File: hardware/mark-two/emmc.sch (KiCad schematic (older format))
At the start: 21 parts, among them U2 MX6UL-VM, U3 EMMC16G

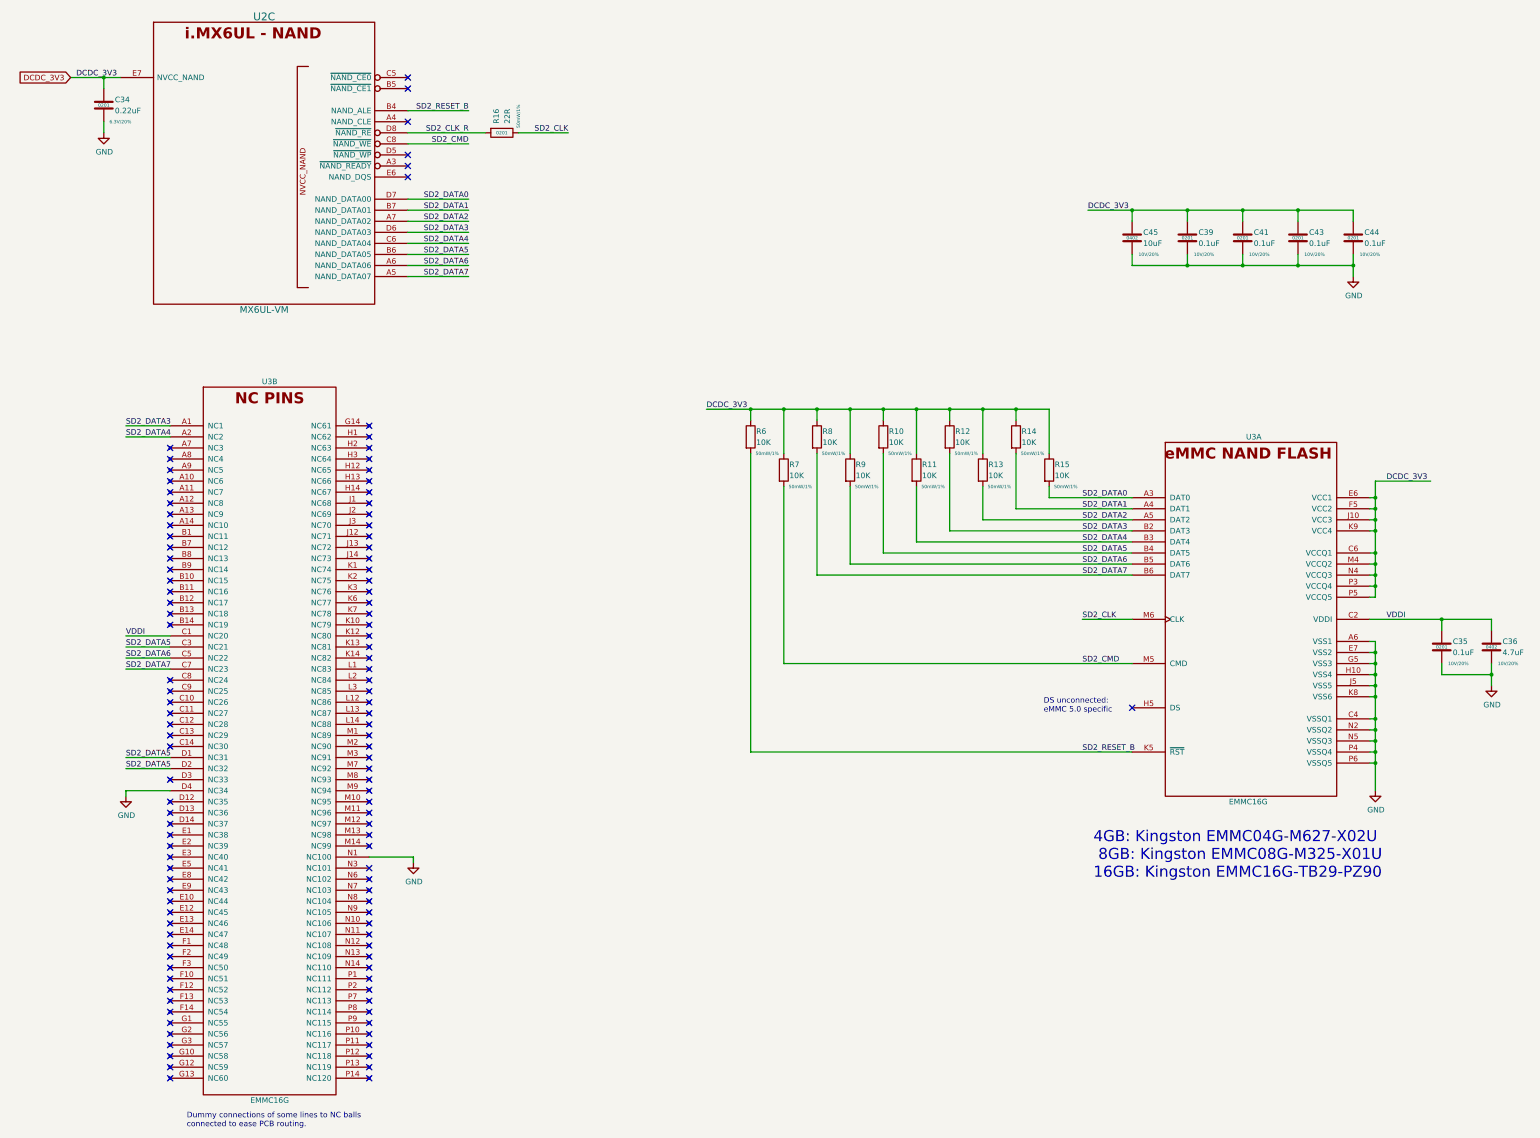
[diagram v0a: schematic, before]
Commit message: add USB armory Mk II rev. γ
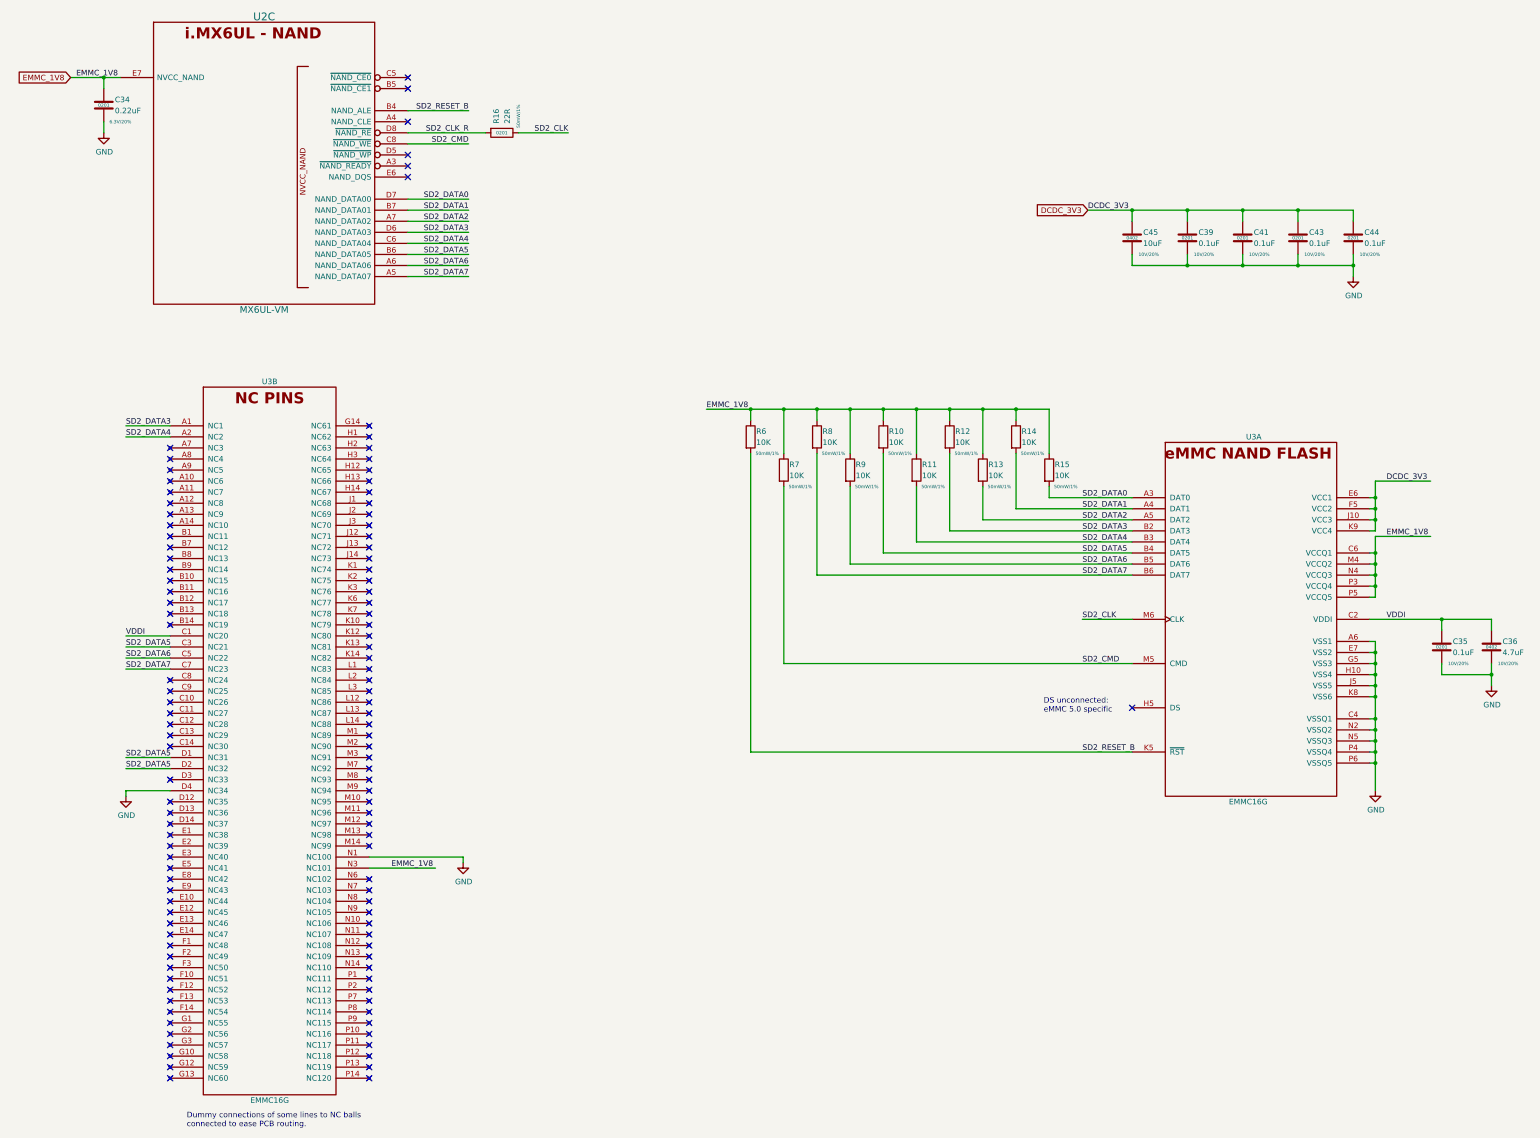
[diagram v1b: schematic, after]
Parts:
- U2: Mfg PN (none) -> MCIMX6Z0DVM09AB
- U3: Alternative PN (none) -> FEMDNN016G-58A43, FEMDRM016G-58A43
- U3: Alternative PN (none) -> FEMDNN016G-58A43, FEMDRM016G-58A43; Mfg PN (none) -> EMMC16G-TB29-PZ90
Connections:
- net DCDC_3V3: no longer C34.1, R10.1, R11.1, R12.1, R13.1, R14.1, R15.1, R6.1, R7.1, R8.1, R9.1, U2.E7 (NVCC_NAND), U3.C6 (VCCQ1), U3.M4 (VCCQ2), U3.N4 (VCCQ3), U3.P3 (VCCQ4), U3.P5 (VCCQ5)
- net EMMC_1V8: now reaches U3.N3 (NC101)
- net EMMC_1V8: now also C34.1, R10.1, R11.1, R12.1, R13.1, R14.1, R15.1, R6.1, R7.1, R8.1, R9.1, U2.E7 (NVCC_NAND), U3.C6 (VCCQ1), U3.M4 (VCCQ2), U3.N4 (VCCQ3), U3.P3 (VCCQ4), U3.P5 (VCCQ5)
- no-connect marks 117 -> 116
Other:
- note removed: "4GB: Kingston EMMC04G-M627-X02U\n 8GB: Kingston EMMC08G-M325-X01U\n16GB: Kingston EMMC16G-TB29-PZ90"
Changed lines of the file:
@@
 EESchema Schematic File Version 4
-LIBS:armory-cache
 EELAYER 30 0
 EELAYER END
@@
 encoding utf-8
 Sheet 3 13
-Title "USB ARMORY"
-Date "2019-06-25"
-Rev "MARK II"
+Title "USB armory Mk II"
+Date "2021-02-18"
+Rev "γ"
 Comp "F-Secure"
-Comment1 "Copyright © 2019 F-Secure"
-Comment2 "License: CERN OHL v1.2"
-Comment3 "https://github.com/inversepath/usbarmory"
+Comment1 "Copyright © F-Secure Corporation"
+Comment2 "License: CERN-OHL-S"
+Comment3 "https://github.com/f-secure-foundry/usbarmory"
 Comment4 ""
 $EndDescr
@@
 F 7 "Avnet" H 12350 4650 50  0001 C CNN "Supplier"
 F 8 "-" H 12350 4650 50  0001 C CNN "Supplier PN"
+F 9 "FEMDNN016G-58A43, FEMDRM016G-58A43 " H 12350 4650 50  0001 C CNN "Alternative PN"
 	1    12350 4650
 	1    0    0    -1
@@
 NoConn ~ 4400 8200
 NoConn ~ 4400 8300
-NoConn ~ 4400 8500
 NoConn ~ 4400 8600
 NoConn ~ 4400 8700
@@
 F 2 "armory-kicad:SOT1534-2" H 3960 -310 60  0001 C CNN
 F 3 "https://www.nxp.com/docs/en/data-sheet/IMX6ULCEC.pdf" H 3960 -310 60  0001 C CNN
+F 4 "MCIMX6Z0DVM09AB" H 3450 850 50  0001 C CNN "Mfg PN"
 	3    3450 850
 	1    0    0    -1
@@
 F 2 "snapeda:FBGA-153" H 3850 4150 50  0001 C CNN
 F 3 "https://media.kingston.com/pdfs/emmc/eMMC_Product_flyer.pdf" H 3850 4150 50  0001 C CNN
+F 4 "FEMDNN016G-58A43, FEMDRM016G-58A43 " H 3500 4150 50  0001 C CNN "Alternative PN"
+F 5 "EMMC16G-TB29-PZ90" H 3500 4150 50  0001 C CNN "Mfg PN"
 	2    3500 4150
 	1    0    0    -1
@@
 	13450 6250 14100 6250
 Text GLabel 1700 1350 0    50   Input ~ 0
-DCDC_3V3
+EMMC_1V8
 Text Label 1750 1350 0    50   ~ 0
-DCDC_3V3
+EMMC_1V8
 $Comp
 L Device:C C?
@@
 L power:GND #PWR?
 U 1 1 5CE566A8
-P 4800 8450
+P 5250 8450
 AR Path="/5BEA6694/5CE566A8" Ref="#PWR?"  Part="1"
 AR Path="/53722D05/5CE566A8" Ref="#PWR0103"  Part="1"
 AR Path="/5C0717D2/5CE566A8" Ref="#PWR?"  Part="1"
-F 0 "#PWR0103" H 4800 8200 50  0001 C CNN
-F 1 "GND" H 4805 8277 50  0000 C CNN
-F 2 "" H 4800 8450 50  0001 C CNN
-F 3 "" H 4800 8450 50  0001 C CNN
-	1    4800 8450
+F 0 "#PWR0103" H 5250 8200 50  0001 C CNN
+F 1 "GND" H 5255 8277 50  0000 C CNN
+F 2 "" H 5250 8450 50  0001 C CNN
+F 3 "" H 5250 8450 50  0001 C CNN
+	1    5250 8450
 	1    0    0    -1
 $EndComp
@@
 	2200 7600 2600 7600
 Text Label 7450 4350 0    50   ~ 0
-DCDC_3V3
+EMMC_1V8
 Text Label 10900 2550 0    50   ~ 0
 DCDC_3V3
@@
 Wire Wire Line
 	2200 7800 2200 7850
-Wire Wire Line
-	4800 8450 4800 8400
-Wire Wire Line
-	4400 8400 4800 8400
 $Comp
 L Device:C C?
@@
 	13500 5950 13500 5850
 Wire Wire Line
-	13500 5450 13500 5650
-Connection ~ 13500 5450
-Connection ~ 13500 5650
-Wire Wire Line
 	13500 5650 13500 5750
 Wire Wire Line
@@
 Wire Wire Line
 	2000 1350 2150 1350
-Text Notes 10950 8600 0    100  ~ 0
- 4GB: Kingston EMMC04G-M627-X02U\n 8GB: Kingston EMMC08G-M325-X01U\n16GB: Kingston EMMC16G-TB29-PZ90
+Text Label 13600 5500 0    50   ~ 0
+EMMC_1V8
+Wire Wire Line
+	13500 5500 14000 5500
+Wire Wire Line
+	13500 5500 13500 5650
+Connection ~ 13500 5650
+Text GLabel 10900 2550 0    50   Input ~ 0
+DCDC_3V3
+Wire Wire Line
+	4400 8500 5000 8500
+Text Label 4600 8500 0    50   ~ 0
+EMMC_1V8
+Wire Wire Line
+	5250 8400 5250 8450
+Wire Wire Line
+	4400 8400 5250 8400
 $EndSCHEMATC
